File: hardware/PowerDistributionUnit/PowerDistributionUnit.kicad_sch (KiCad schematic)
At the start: 100 parts, among them J1 973582101, J2 973582100, J3 973582101, J4 973582100, Q1 SQJ141ELP, Q2 CSD18511Q5A, SW1 SW_Push, U1 TPS25983, U2 AD5258, U3 NUCLEO_L432KC

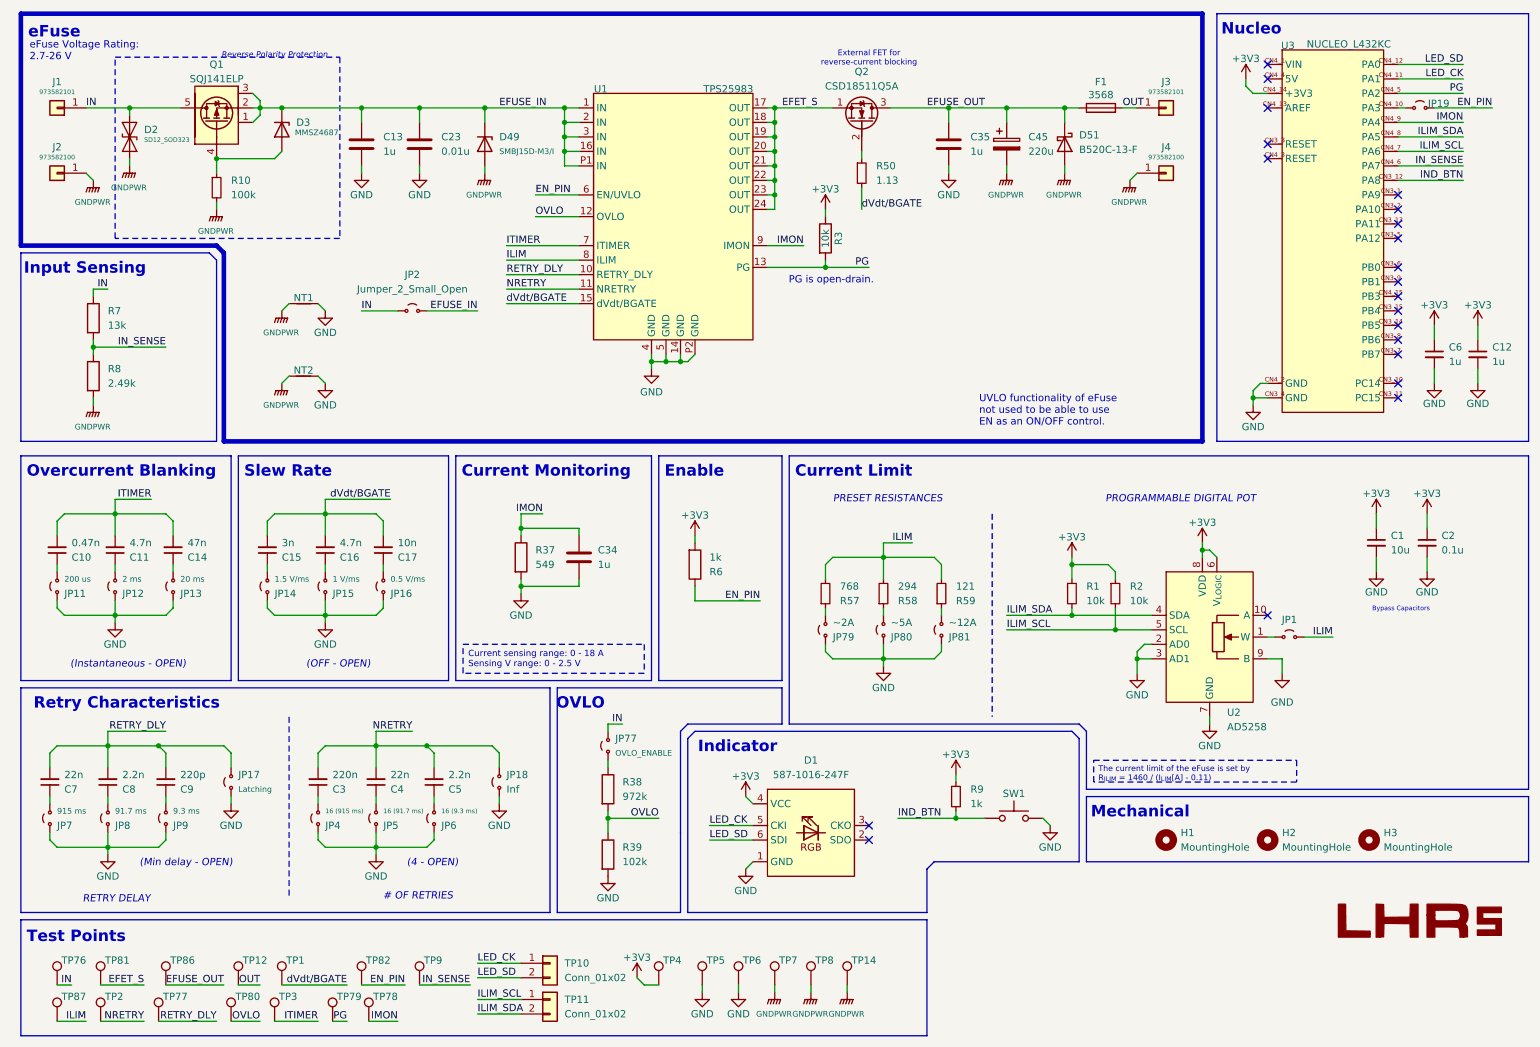
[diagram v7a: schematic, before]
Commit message: Changed a gnd pwr tp to gnd. Reduced capacitor value at output. Changed pwr gnd to gnd for input resistor divider.
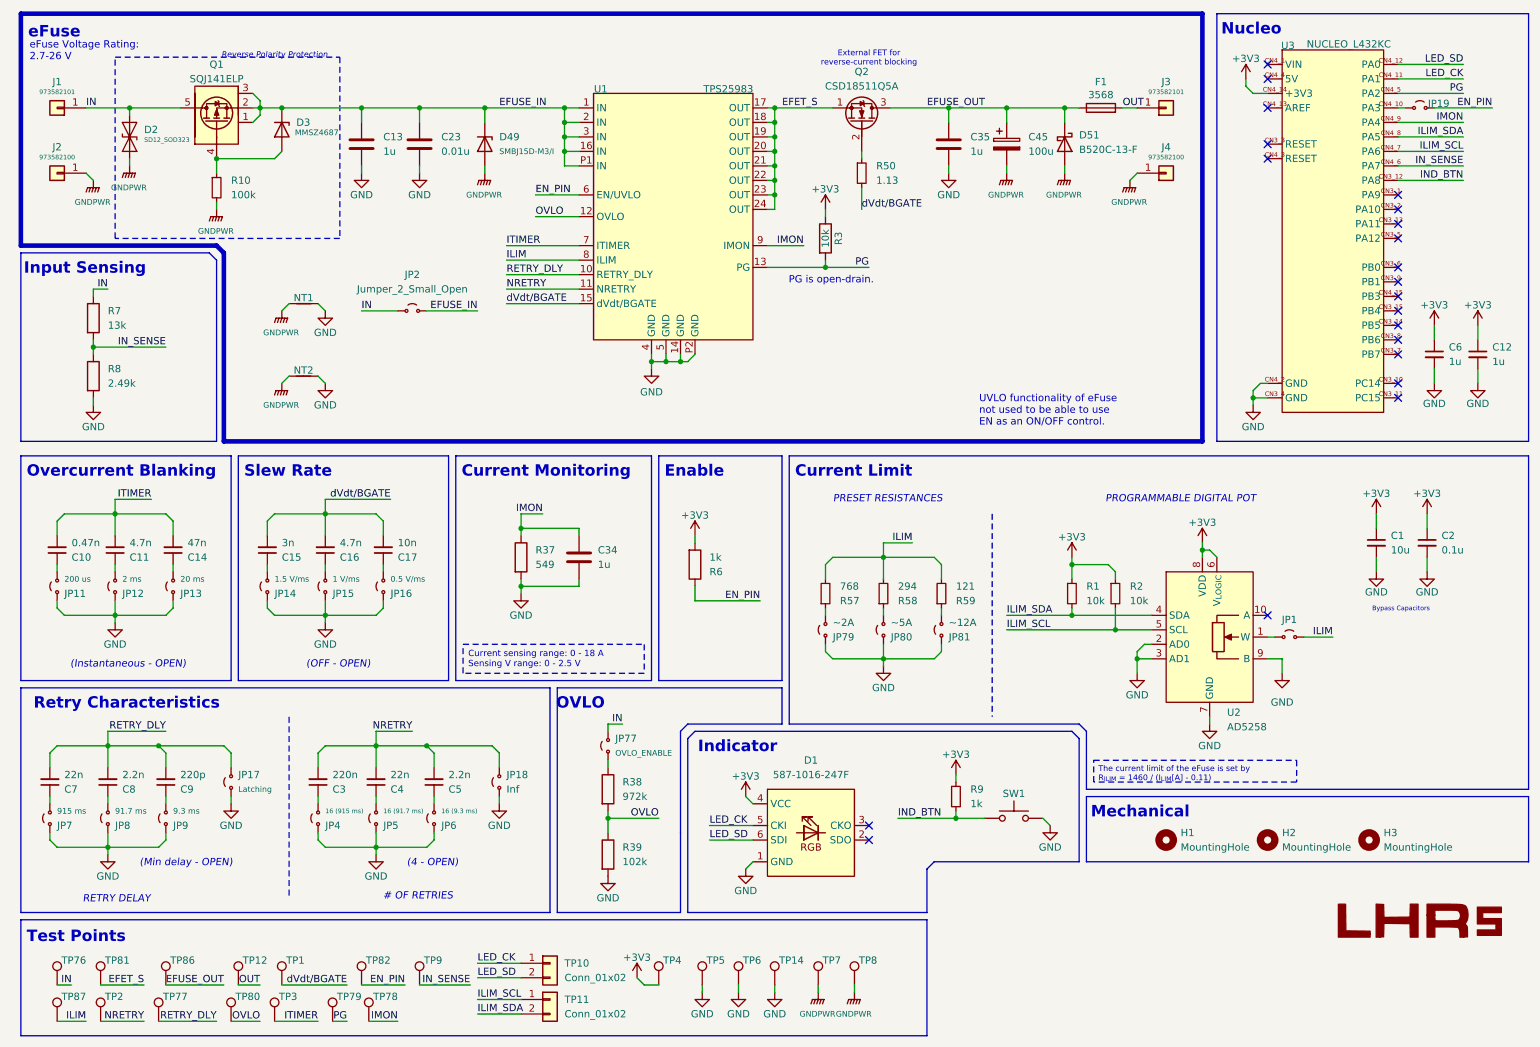
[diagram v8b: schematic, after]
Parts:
- C45: value 220u -> 100u; footprint Capacitor_SMD:CP_Elec_10x12.6 -> Capacitor_SMD:CP_Elec_6.3x9.9
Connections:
- net GND: now also R8.2, TP14.1
- net GNDPWR: no longer R8.2, TP14.1
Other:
- moved on the sheet: TP14, TP7, TP8
